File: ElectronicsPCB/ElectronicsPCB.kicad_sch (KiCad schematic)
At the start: 30 parts

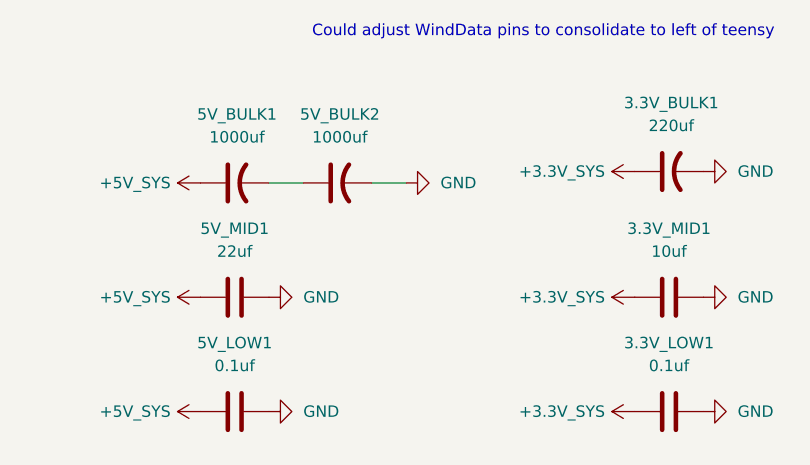
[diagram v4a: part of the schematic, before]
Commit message: caps should be in parallel not series
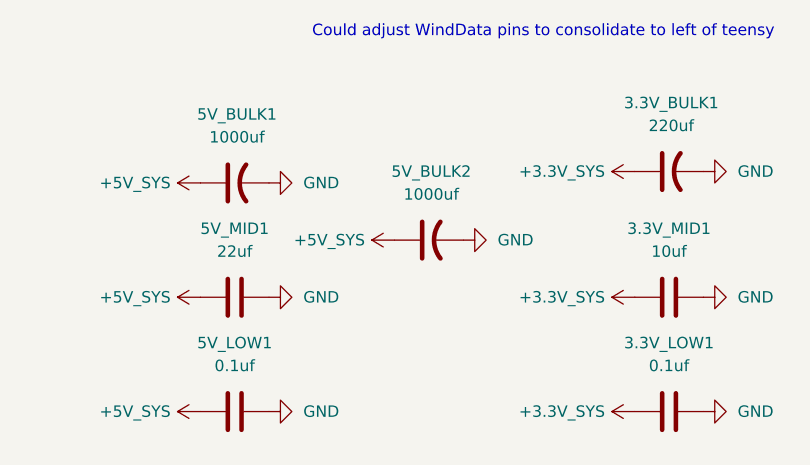
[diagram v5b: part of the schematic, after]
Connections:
- net +5V_SYS: now also 5V_BULK2.1
- net GND: now also 5V_BULK1.2
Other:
- moved on the sheet: 5V_BULK2
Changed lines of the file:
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@@
 	(wire
 		(pts
-			(xy 189.23 33.02) (xy 193.04 33.02)
-		)
-		(stroke
-			(width 0)
-			(type default)
-		)
-	)
-	(wire
-		(pts
 			(xy 58.42 41.91) (xy 78.74 41.91)
 		)
@@
 	(wire
 		(pts
-			(xy 177.8 33.02) (xy 181.61 33.02)
-		)
-		(stroke
-			(width 0)
-			(type default)
-		)
-	)
-	(wire
-		(pts
 			(xy 76.2 31.75) (xy 78.74 31.75)
 		)
@@
 	)
 	(symbol
+		(lib_id "power:GND")
+		(at 177.8 33.02 90)
+		(unit 1)
+		(exclude_from_sim no)
+		(in_bom yes)
+		(on_board yes)
+		(dnp no)
+		(fields_autoplaced yes)
+		(property "Reference" "#PWR059"
+			(at 184.15 33.02 0)
+			(effects
+				(font
+					(size 1.27 1.27)
+				)
+				(hide yes)
+			)
+		)
+		(property "Value" "GND"
+			(at 181.61 33.0199 90)
+			(effects
+				(font
+					(size 1.27 1.27)
+				)
+				(justify right)
+			)
+		)
+		(property "Footprint" ""
+			(at 177.8 33.02 0)
+			(effects
+				(font
+					(size 1.27 1.27)
+				)
+				(hide yes)
+			)
+		)
+		(property "Datasheet" ""
+			(at 177.8 33.02 0)
+			(effects
+				(font
+					(size 1.27 1.27)
+				)
+				(hide yes)
+			)
+		)
+		(property "Description" "Power symbol creates a global label with name \"GND\" , ground"
+			(at 177.8 33.02 0)
+			(effects
+				(font
+					(size 1.27 1.27)
+				)
+				(hide yes)
+			)
+		)
+		(pin "1"
+		)
+		(instances
+			(project "ElectronicsPCB"
+				(path "/986f98f1-de62-46c2-9c6e-8a3d3d9a8a4d"
+					(reference "#PWR059")
+					(unit 1)
+				)
+			)
+		)
+	)
+	(symbol
 		(lib_id "Mechanical:MountingHole")
 		(at 212.09 81.28 0)
@@
 	)
 	(symbol
+		(lib_id "power:+24V")
+		(at 191.77 39.37 90)
+		(unit 1)
+		(exclude_from_sim no)
+		(in_bom yes)
+		(on_board yes)
+		(dnp no)
+		(property "Reference" "#PWR060"
+			(at 195.58 39.37 0)
+			(effects
+				(font
+					(size 1.27 1.27)
+				)
+				(hide yes)
+			)
+		)
+		(property "Value" "+5V_SYS"
+			(at 188.468 39.37 90)
+			(effects
+				(font
+					(size 1.27 1.27)
+				)
+				(justify left)
+			)
+		)
+		(property "Footprint" ""
+			(at 191.77 39.37 0)
+			(effects
+				(font
+					(size 1.27 1.27)
+				)
+				(hide yes)
+			)
+		)
+		(property "Datasheet" ""
+			(at 191.77 39.37 0)
+			(effects
+				(font
+					(size 1.27 1.27)
+				)
+				(hide yes)
+			)
+		)
+		(property "Description" "Power symbol creates a global label with name \"+24V\""
+			(at 191.77 39.37 0)
+			(effects
+				(font
+					(size 1.27 1.27)
+				)
+				(hide yes)
+			)
+		)
+		(pin "1"
+		)
+		(instances
+			(project "ElectronicsPCB"
+				(path "/986f98f1-de62-46c2-9c6e-8a3d3d9a8a4d"
+					(reference "#PWR060")
+					(unit 1)
+				)
+			)
+		)
+	)
+	(symbol
 		(lib_id "power:+3.3V")
 		(at 255.27 135.89 90)
@@
 	(symbol
 		(lib_id "power:GND")
-		(at 193.04 33.02 90)
+		(at 199.39 39.37 90)
 		(unit 1)
 		(exclude_from_sim no)
@@
 		(fields_autoplaced yes)
 		(property "Reference" "#PWR048"
-			(at 199.39 33.02 0)
+			(at 205.74 39.37 0)
 			(effects
 				(font
@@
 		)
 		(property "Value" "GND"
-			(at 196.85 33.0199 90)
+			(at 203.2 39.3699 90)
 			(effects
 				(font
@@
 		)
 		(property "Footprint" ""
-			(at 193.04 33.02 0)
+			(at 199.39 39.37 0)
 			(effects
 				(font
@@
 		)
 		(property "Datasheet" ""
-			(at 193.04 33.02 0)
+			(at 199.39 39.37 0)
 			(effects
 				(font
@@
 		)
 		(property "Description" "Power symbol creates a global label with name \"GND\" , ground"
-			(at 193.04 33.02 0)
+			(at 199.39 39.37 0)
 			(effects
 				(font
@@
 	(symbol
 		(lib_id "Device:C_US")
-		(at 185.42 33.02 90)
+		(at 195.58 39.37 90)
 		(unit 1)
 		(exclude_from_sim no)
@@
 		(fields_autoplaced yes)
 		(property "Reference" "5V_BULK2"
-			(at 185.674 25.4 90)
+			(at 195.834 31.75 90)
 			(effects
 				(font
@@
 		)
 		(property "Value" "1000uf"
-			(at 185.674 27.94 90)
+			(at 195.834 34.29 90)
 			(effects
 				(font
@@
 		)
 		(property "Footprint" "ElectronicsFootprints:CAP_EEE1A_1000uf"
-			(at 185.42 33.02 0)
+			(at 195.58 39.37 0)
 			(effects
 				(font
@@
 		)
 		(property "Datasheet" ""
-			(at 185.42 33.02 0)
+			(at 195.58 39.37 0)
 			(effects
 				(font
@@
 		)
 		(property "Description" "capacitor, US symbol"
-			(at 185.42 33.02 0)
+			(at 195.58 39.37 0)
 			(effects
 				(font
